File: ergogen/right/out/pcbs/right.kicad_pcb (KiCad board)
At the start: 2 copper layers, 115 x 95 mm, 46 parts

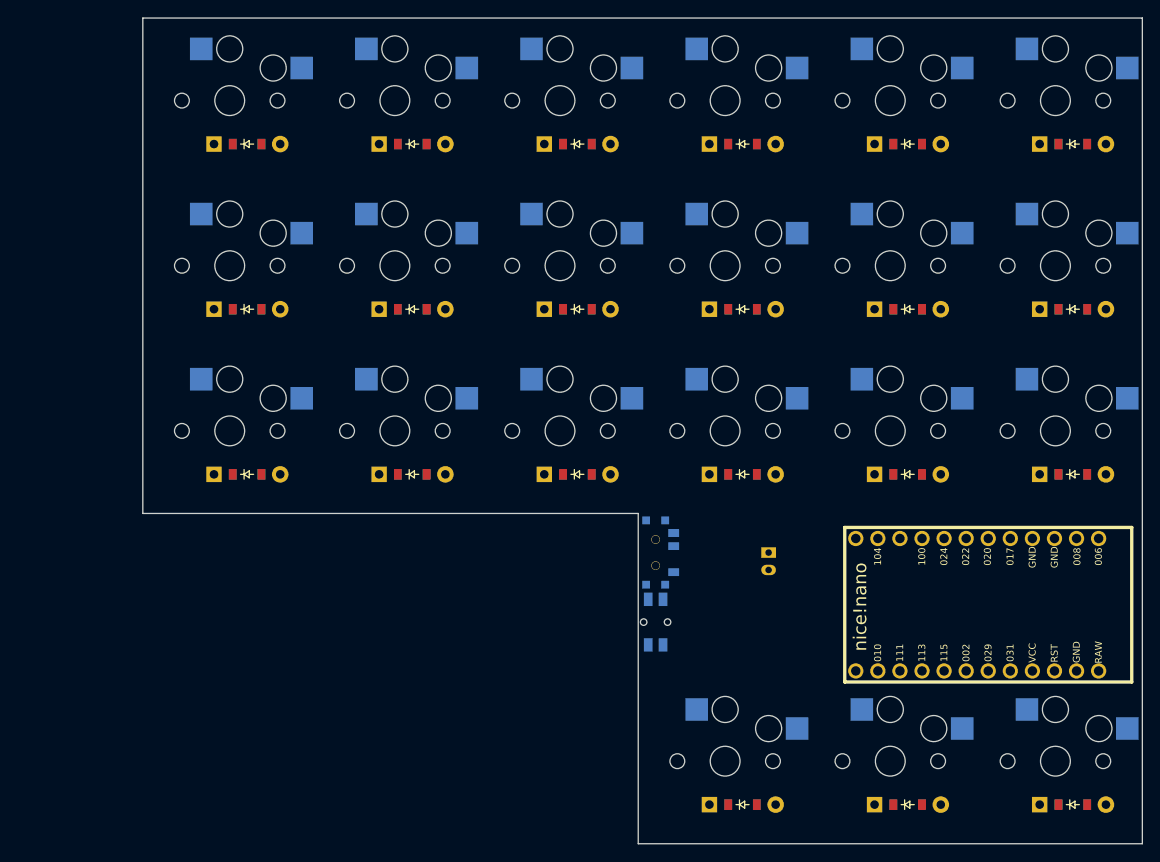
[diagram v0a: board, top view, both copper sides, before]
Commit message: fix: Right part paddings.
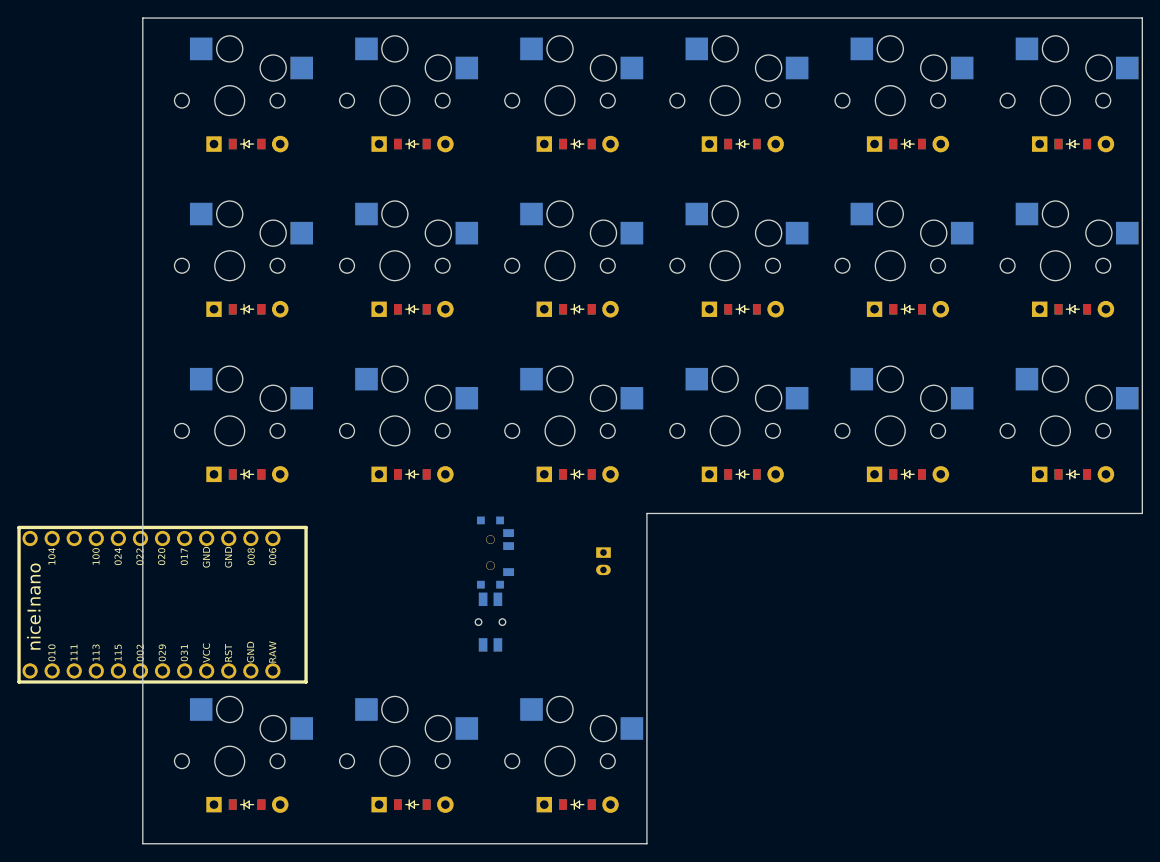
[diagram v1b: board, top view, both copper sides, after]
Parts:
- moved MCU1 95.0 mm to (91.0, 132.0)
- moved D18 78.3 mm to (178.0, 79.0)
- moved S18 78.3 mm to (176.0, 74.0)
- moved D9 76.0 mm to (140.0, 155.0)
- moved S9 76.0 mm to (138.0, 150.0)
- moved D14 60.1 mm to (159.0, 98.0)
- moved S14 60.1 mm to (157.0, 93.0)
- moved D5 57.0 mm to (121.0, 155.0)
- moved S5 57.0 mm to (119.0, 150.0)
- moved D10 42.5 mm to (140.0, 117.0)
- moved D15 42.5 mm to (159.0, 79.0)
- moved D4 42.5 mm to (102.0, 79.0)
- moved S10 42.5 mm to (138.0, 112.0)
- moved S15 42.5 mm to (157.0, 74.0)
- moved S4 42.5 mm to (100.0, 74.0)
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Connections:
- D1 pad 1: P011 -> P010
- D1 pad 2: outer_bottom -> inner_thumb
- D10 pad 1: P010 -> P011
- D10 pad 2: middle_thumb -> middle_bottom
- D11 pad 1: P011 -> P100
- D11 pad 2: middle_bottom -> middle_home
- D12 pad 1: P100 -> P024
- D12 pad 2: middle_home -> middle_top
- D13 pad 1: P024 -> P011
- D13 pad 2: middle_top -> ring_bottom
- D14 pad 1: P010 -> P100
- D14 pad 2: index_thumb -> ring_home
- D15 pad 1: P011 -> P024
- D15 pad 2: index_bottom -> ring_top
- D16 pad 1: P100 -> P011
- D16 pad 2: index_home -> pinky_bottom
- D17 pad 1: P024 -> P100
- D17 pad 2: index_top -> pinky_home
- D18 pad 1: P010 -> P024
- D18 pad 2: inner_thumb -> pinky_top
- D19 pad 2: inner_bottom -> outer_bottom
- D2 pad 1: P100 -> P011
- D2 pad 2: outer_home -> inner_bottom
- D20 pad 2: inner_home -> outer_home
- D21 pad 2: inner_top -> outer_top
- D3 pad 1: P024 -> P100
- D3 pad 2: outer_top -> inner_home
- D4 pad 1: P011 -> P024
- D4 pad 2: pinky_bottom -> inner_top
- D5 pad 1: P100 -> P010
- D5 pad 2: pinky_home -> index_thumb
- D6 pad 1: P024 -> P011
- D6 pad 2: pinky_top -> index_bottom
- D7 pad 1: P011 -> P100
- D7 pad 2: ring_bottom -> index_home
- D8 pad 1: P100 -> P024
- D8 pad 2: ring_home -> index_top
- D9 pad 1: P024 -> P010
- D9 pad 2: ring_top -> middle_thumb
- S1 pad 2: outer_bottom -> inner_thumb
- S10 pad 1: P113 -> P017
- S10 pad 2: middle_thumb -> middle_bottom
- S11 pad 1: P113 -> P017
- S11 pad 2: middle_bottom -> middle_home
- S12 pad 1: P113 -> P017
- S12 pad 2: middle_home -> middle_top
- S13 pad 2: middle_top -> ring_bottom
- S14 pad 1: P111 -> P113
- S14 pad 2: index_thumb -> ring_home
- S15 pad 1: P111 -> P113
- S15 pad 2: index_bottom -> ring_top
- S16 pad 2: index_home -> pinky_bottom
- S17 pad 2: index_top -> pinky_home
- S18 pad 1: P115 -> P111
- S18 pad 2: inner_thumb -> pinky_top
- S19 pad 2: inner_bottom -> outer_bottom
- S2 pad 2: outer_home -> inner_bottom
- S20 pad 2: inner_home -> outer_home
- S21 pad 2: inner_top -> outer_top
- S3 pad 2: outer_top -> inner_home
- S4 pad 1: P020 -> P022
- S4 pad 2: pinky_bottom -> inner_top
- S5 pad 2: pinky_home -> index_thumb
- S6 pad 2: pinky_top -> index_bottom
- S7 pad 1: P017 -> P020
- S7 pad 2: ring_bottom -> index_home
- S8 pad 1: P017 -> P020
- S8 pad 2: ring_home -> index_top
- S9 pad 2: ring_top -> middle_thumb
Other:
- outline, holes or cut-outs redrawn

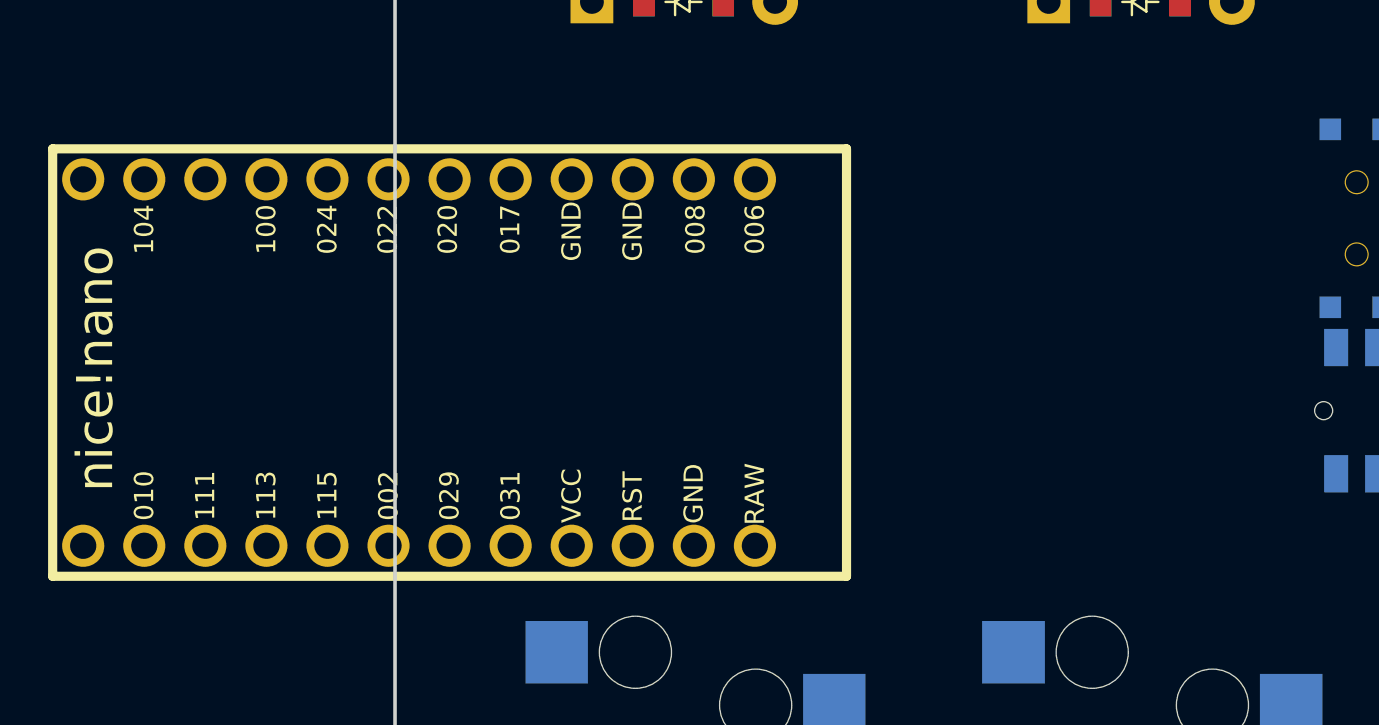
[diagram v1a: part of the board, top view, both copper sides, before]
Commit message: fix: MCU position
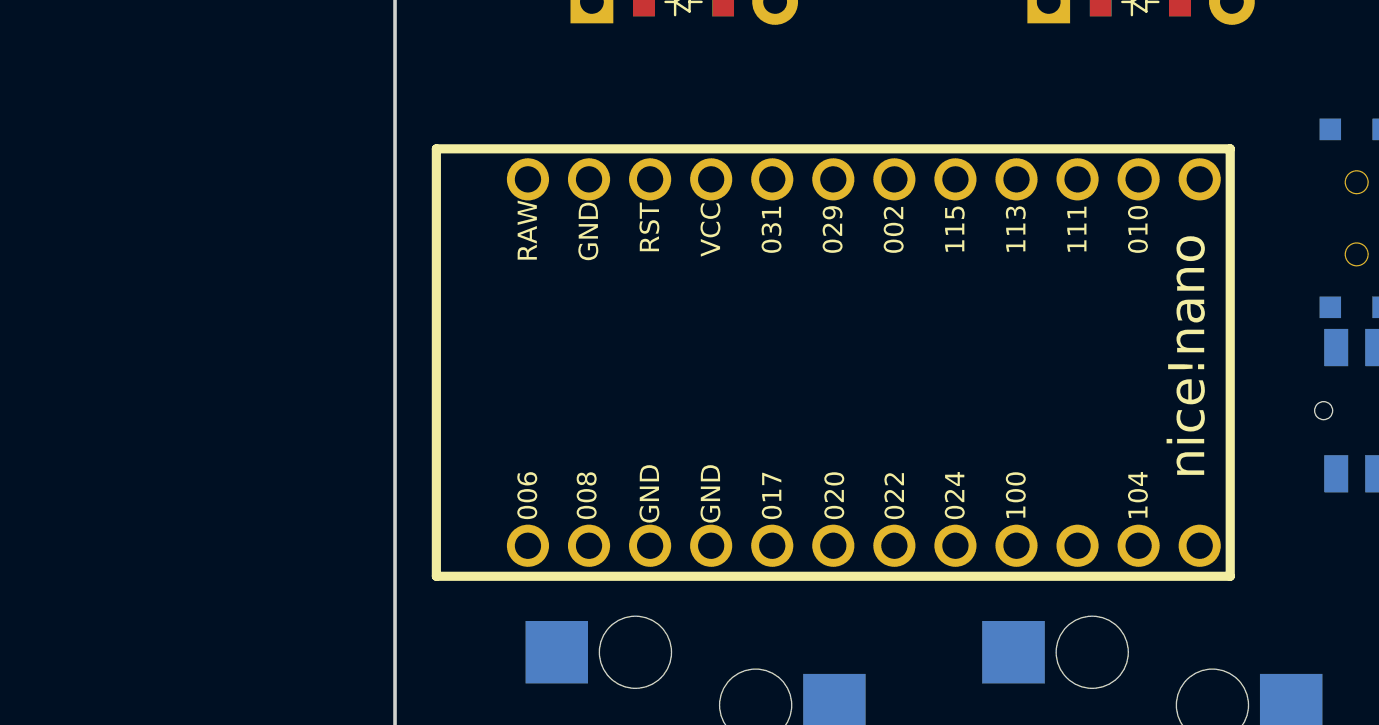
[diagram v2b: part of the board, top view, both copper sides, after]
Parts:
- moved MCU1 18.5 mm to (109.5, 132.0), turned to 0 degrees

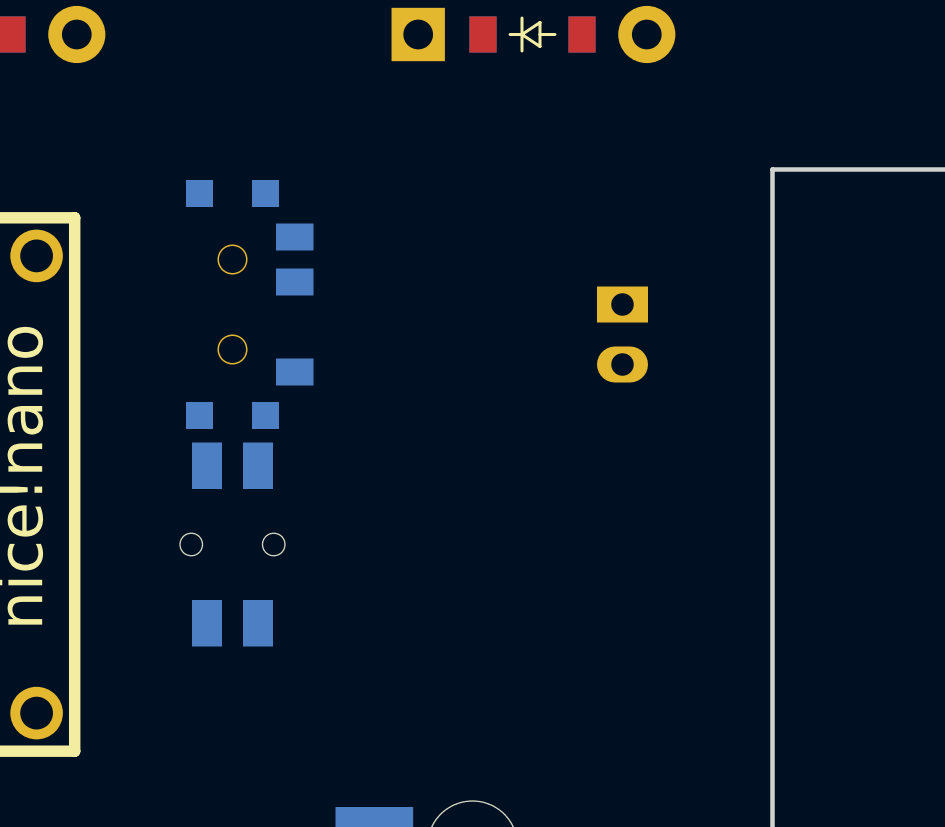
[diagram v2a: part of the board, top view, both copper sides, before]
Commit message: fix: Buttons position
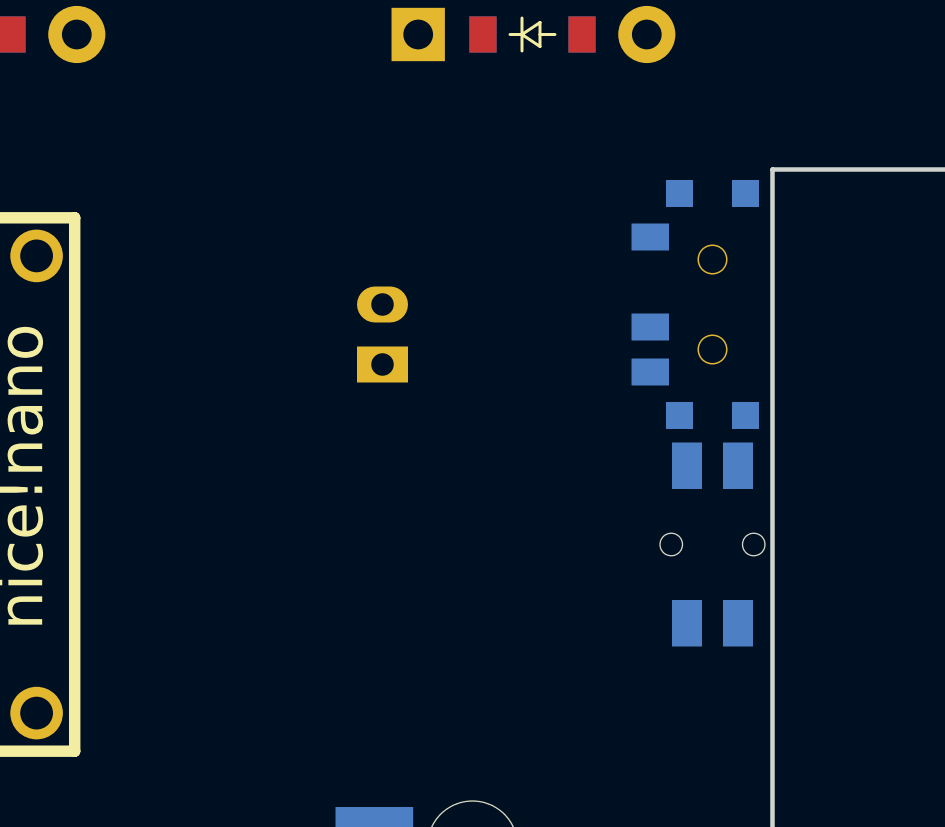
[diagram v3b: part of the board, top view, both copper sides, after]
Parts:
- moved B1 16.0 mm to (146.0, 134.0), turned to -90 degrees
- moved T1 16.0 mm to (146.0, 126.0), turned to -90 degrees
- moved JST1 8.00 mm to (135.0, 127.0), turned to 90 degrees
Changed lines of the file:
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@@
         (descr "JST PH series connector, S2B-PH-K, side entry type, through hole, Datasheet: http://www.jst-mfg.com/product/pdf/eng/ePH.pdf")
         (tags "connector jst ph")
-        (at 143 127 -90)
+        (at 135 127 90)
         (fp_text reference "JST1" (at 0 0) (layer F.SilkS) hide (effects (font (size 1.27 1.27) (thickness 0.15))))
         (fp_text value "" (at 0 0) (layer F.SilkS) hide (effects (font (size 1.27 1.27) (thickness 0.15))))
@@
         (fp_line (start -1 1.5) (end -1 2.0) (layer B.SilkS) (width 0.15))
         (fp_line (start -1.25 1.75) (end -0.75 1.75) (layer B.SilkS) (width 0.15))
-        (pad 1 thru_hole rect (at -1 0 -90) (size 1.2 1.7) (drill 0.75) (layers *.Cu *.Mask) (net 44 "pos"))
-        (pad 2 thru_hole oval (at 1 0 -90) (size 1.2 1.7) (drill 0.75) (layers *.Cu *.Mask) (net 33 "GND"))
+        (pad 1 thru_hole rect (at -1 0 90) (size 1.2 1.7) (drill 0.75) (layers *.Cu *.Mask) (net 44 "pos"))
+        (pad 2 thru_hole oval (at 1 0 90) (size 1.2 1.7) (drill 0.75) (layers *.Cu *.Mask) (net 33 "GND"))
     )
     (module Panasonic_EVQPUL_EVQPUC (layer F.Cu)
         (descr "http://industrial.panasonic.com/cdbs/www-data/pdf/ATV0000/ATV0000CE5.pdf")
         (tags "SMD SMT SPST EVQPUL EVQPUC")
-        (at 130 134 90)
+        (at 146 134 -90)
         (fp_text reference "B1" (at 0 0) (layer "F.SilkS") hide (effects (font (size 1 1) (thickness 0.15))))
         (fp_text value "Panasonic_EVQPUL_EVQPUC" (at 0 3.5) (layer "F.Fab") hide (effects (font (size 1 1) (thickness 0.15))))
@@
         (fp_line (start 2.35 1.75) (end -2.35 1.75) (stroke (width 0.1) (type solid)) (layer "B.Fab"))
         (fp_line (start 2.35 1.75) (end 2.35 -1.75) (stroke (width 0.1) (type solid)) (layer "B.Fab"))
-        (pad "" np_thru_hole circle (at 0 -1.375 90) (size 0.75 0.75) (drill 0.75) (layers "*.Cu" "*.Mask"))
-        (pad "" np_thru_hole circle (at 0 1.375 90) (size 0.75 0.75) (drill 0.75) (layers "*.Cu" "*.Mask"))
-        (pad "1" smd rect (at -2.625 -0.85 90) (size 1.55 1) (layers "B.Cu" "B.Paste" "B.Mask") (net 33 "GND"))
-        (pad "1" smd rect (at 2.625 -0.85 90) (size 1.55 1) (layers "B.Cu" "B.Paste" "B.Mask") (net 33 "GND"))
-        (pad "2" smd rect (at -2.625 0.85 90) (size 1.55 1) (layers "B.Cu" "B.Paste" "B.Mask") (net 34 "RST"))
-        (pad "2" smd rect (at 2.625 0.85 90) (size 1.55 1) (layers "B.Cu" "B.Paste" "B.Mask") (net 34 "RST"))
+        (pad "" np_thru_hole circle (at 0 -1.375 -90) (size 0.75 0.75) (drill 0.75) (layers "*.Cu" "*.Mask"))
+        (pad "" np_thru_hole circle (at 0 1.375 -90) (size 0.75 0.75) (drill 0.75) (layers "*.Cu" "*.Mask"))
+        (pad "1" smd rect (at -2.625 -0.85 -90) (size 1.55 1) (layers "B.Cu" "B.Paste" "B.Mask") (net 33 "GND"))
+        (pad "1" smd rect (at 2.625 -0.85 -90) (size 1.55 1) (layers "B.Cu" "B.Paste" "B.Mask") (net 33 "GND"))
+        (pad "2" smd rect (at -2.625 0.85 -90) (size 1.55 1) (layers "B.Cu" "B.Paste" "B.Mask") (net 34 "RST"))
+        (pad "2" smd rect (at 2.625 0.85 -90) (size 1.55 1) (layers "B.Cu" "B.Paste" "B.Mask") (net 34 "RST"))
     )
         (module E73:SPDT_C128955 (layer F.Cu)
-            (at 130 126 90)
+            (at 146 126 -90)
             (fp_text reference "T1" (at 0 0) (layer F.SilkS) hide (effects (font (size 1.27 1.27) (thickness 0.15))))
             (fp_text value "" (at 0 0) (layer F.SilkS) hide (effects (font (size 1.27 1.27) (thickness 0.15))))
@@
             (pad "" np_thru_hole circle (at 1.5 0) (size 1 1) (drill 0.9) (layers *.Cu *.Mask))
             (pad "" np_thru_hole circle (at -1.5 0) (size 1 1) (drill 0.9) (layers *.Cu *.Mask))
-            (pad 1 smd rect (at -2.25 2.075 90) (size 0.9 1.25) (layers B.Cu B.Paste B.Mask) (net 44 "pos"))
-            (pad 2 smd rect (at 0.75 2.075 90) (size 0.9 1.25) (layers B.Cu B.Paste B.Mask) (net 32 "RAW"))
-            (pad 3 smd rect (at 2.25 2.075 90) (size 0.9 1.25) (layers B.Cu B.Paste B.Mask))
-            (pad "" smd rect (at 3.7 -1.1 90) (size 0.9 0.9) (layers B.Cu B.Paste B.Mask))
-            (pad "" smd rect (at 3.7 1.1 90) (size 0.9 0.9) (layers B.Cu B.Paste B.Mask))
-            (pad "" smd rect (at -3.7 1.1 90) (size 0.9 0.9) (layers B.Cu B.Paste B.Mask))
-            (pad "" smd rect (at -3.7 -1.1 90) (size 0.9 0.9) (layers B.Cu B.Paste B.Mask))
+            (pad 1 smd rect (at -2.25 2.075 -90) (size 0.9 1.25) (layers B.Cu B.Paste B.Mask) (net 44 "pos"))
+            (pad 2 smd rect (at 0.75 2.075 -90) (size 0.9 1.25) (layers B.Cu B.Paste B.Mask) (net 32 "RAW"))
+            (pad 3 smd rect (at 2.25 2.075 -90) (size 0.9 1.25) (layers B.Cu B.Paste B.Mask))
+            (pad "" smd rect (at 3.7 -1.1 -90) (size 0.9 0.9) (layers B.Cu B.Paste B.Mask))
+            (pad "" smd rect (at 3.7 1.1 -90) (size 0.9 0.9) (layers B.Cu B.Paste B.Mask))
+            (pad "" smd rect (at -3.7 1.1 -90) (size 0.9 0.9) (layers B.Cu B.Paste B.Mask))
+            (pad "" smd rect (at -3.7 -1.1 -90) (size 0.9 0.9) (layers B.Cu B.Paste B.Mask))
         )
   (gr_line (start 90 64.5) (end 205 64.5) (angle 90) (layer Edge.Cuts) (width 0.15))

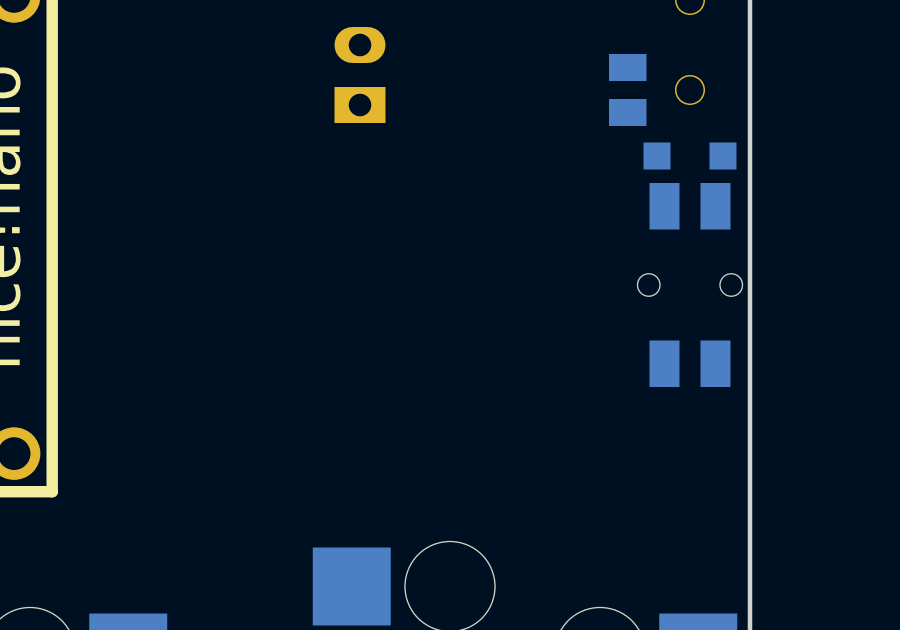
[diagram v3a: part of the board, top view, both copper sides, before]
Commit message: feat: Add mounting hole to the right.
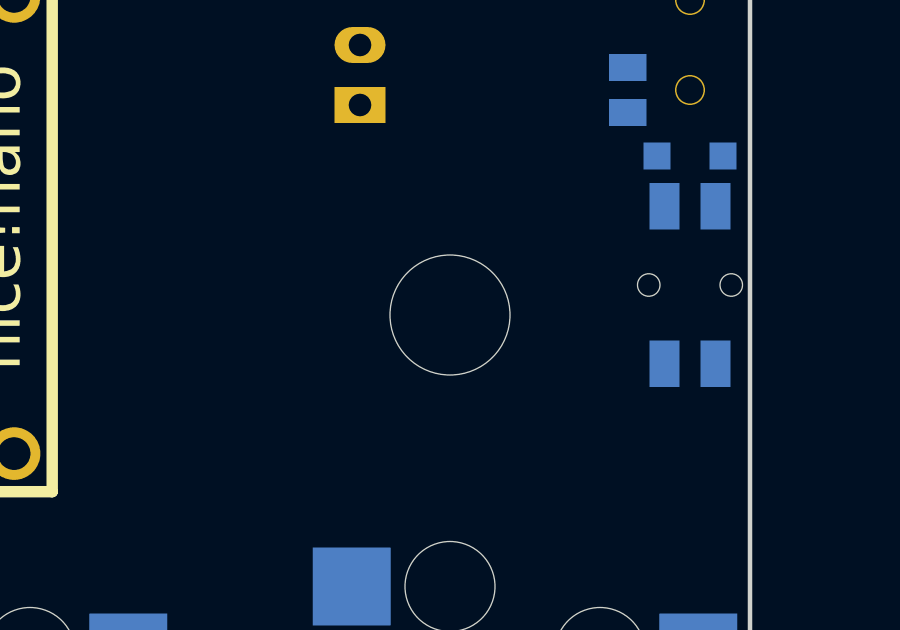
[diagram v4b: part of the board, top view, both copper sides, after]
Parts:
- added ?: , HOLE_M2_TH, F.Cu at (138.0, 135.0)
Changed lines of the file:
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@@
             (pad "" smd rect (at -3.7 -1.1 -90) (size 0.9 0.9) (layers B.Cu B.Paste B.Mask))
         )
+    (module HOLE_M2_TH (layer F.Cu)
+      (at 138 135 0)
+      (pad "" np_thru_hole circle (at 0 0 90) (size 4.0 4.0) (drill 4.0) (layers *.Cu *.Mask F.SilkS) (clearance 0.3)))
   (gr_line (start 90 64.5) (end 205 64.5) (angle 90) (layer Edge.Cuts) (width 0.15))
 (gr_line (start 205 64.5) (end 205 121.5) (angle 90) (layer Edge.Cuts) (width 0.15))
